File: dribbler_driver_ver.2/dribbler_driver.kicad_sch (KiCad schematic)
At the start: 93 parts, among them J1 SWD_Debug, J2 Conn_01x08, J3 Conn_01x02_MountingPin, J4 Conn_01x02_MountingPin, Q1 WSD4070DN, Q10 WSD4070DN, Q2 WSD4070DN, Q5 WSD4070DN, Q6 WSD4070DN, Q9 WSD4070DN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

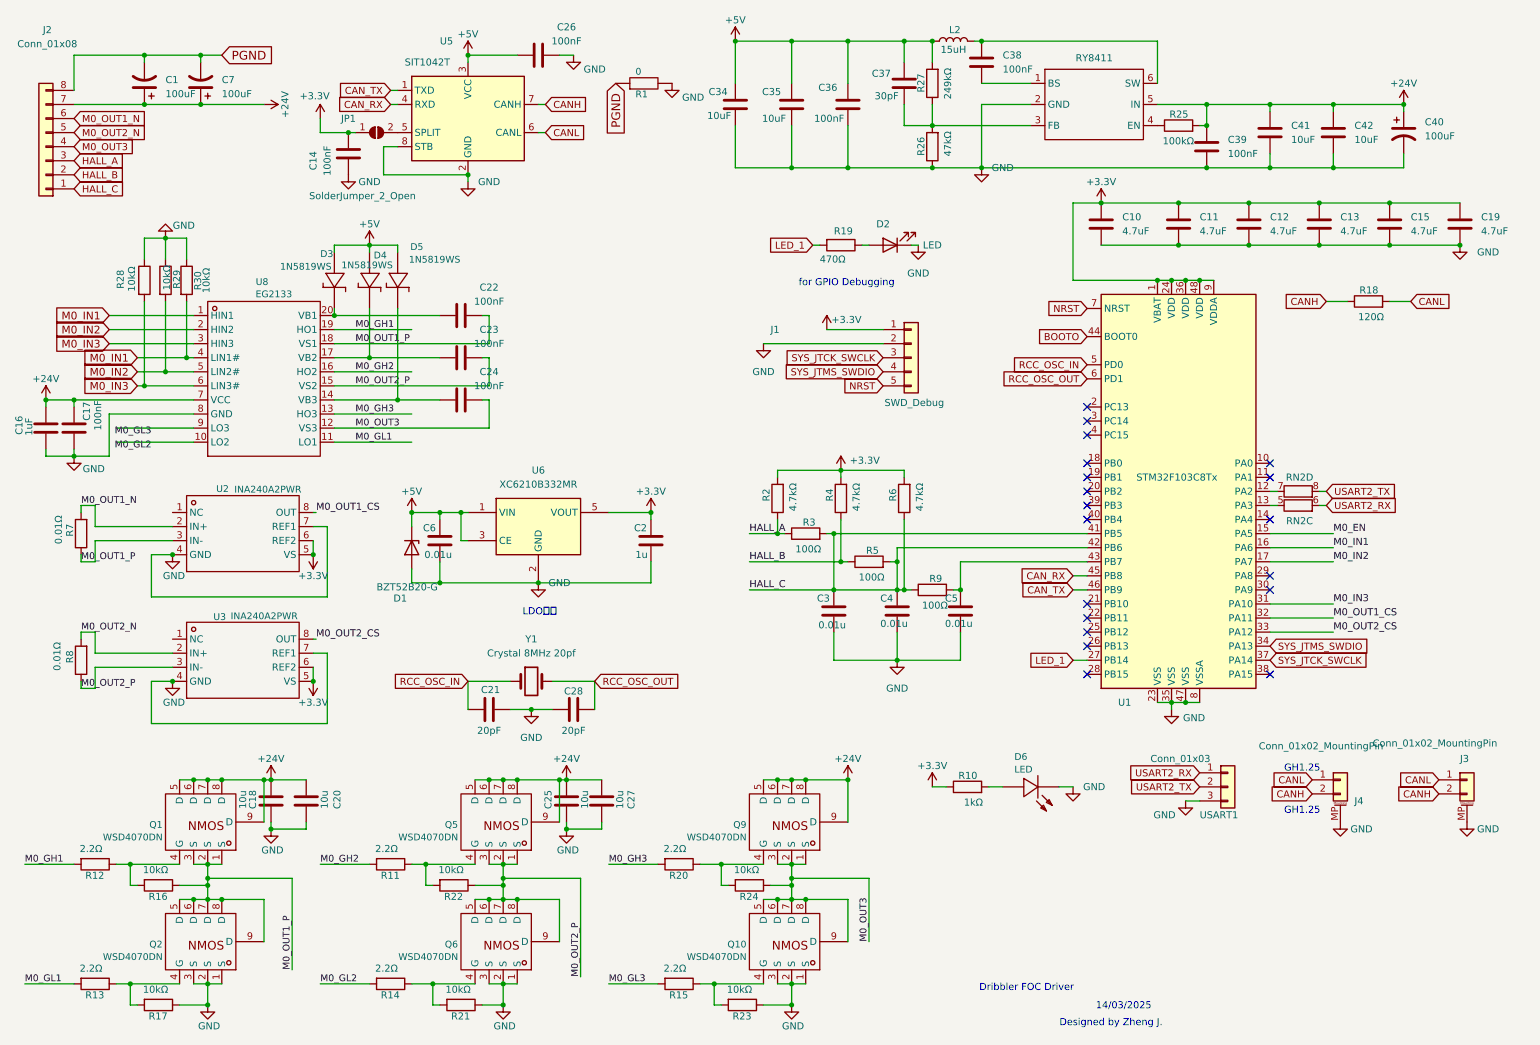
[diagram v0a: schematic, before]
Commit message: fixed stm32 peripherals
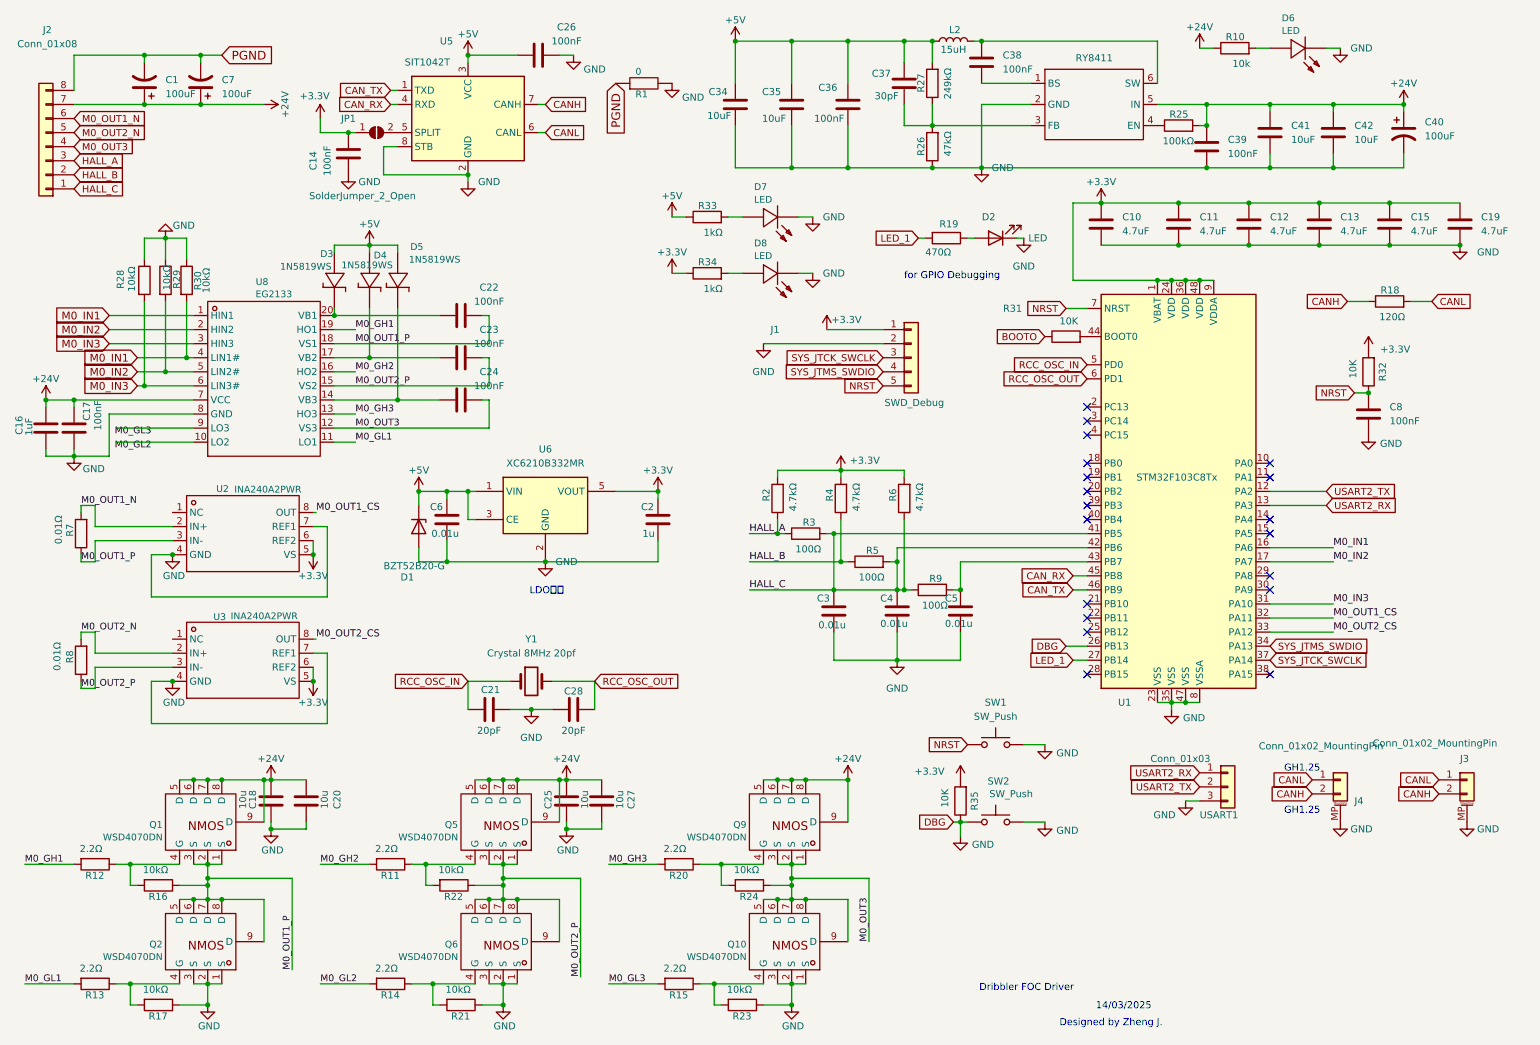
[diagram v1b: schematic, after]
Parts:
- removed RN2: R_Pack04_SIP_Split, R_array_4:0402*4_r, symbol Device:R_Pack04_SIP_Split
- added C8: 100nF, symbol Device:C
- added D7, D8: LED, LED_SMD:LED_0603_1608Metric_Pad1.05x0.95mm_HandSolder, symbol SCH_DengFO-easyedapro:17-21SUYC/TR8
- added R31, R32, R35: 10K, symbol Device:R
- added R33, R34: 1kΩ, Resistor_SMD:R_0603_1608Metric_Pad0.98x0.95mm_HandSolder, symbol Device:R
- added SW1, SW2: SW_Push, symbol Switch:SW_Push
- R10: value 1kΩ -> 10k
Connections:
- net +24V: now also R10.1
- net +3.3V: now also R32.2, R34.1, R35.2; no longer R10.1
- net +5V: now also R33.1
- net BOOTO: now also R31.1; no longer U1.44 (BOOT0)
- net GND: now also U1.26 (PB13), C8.2, D7.1 (-), D8.1 (-), R35.1, SW1.2, SW2.1, SW2.2
- net NRST: now also C8.1, R32.1, SW1.1
- net USART2_RX: now also U1.13 (PA3)
- net USART2_TX: now also U1.12 (PA2)
- net M0_EN: no longer names the net of U1.15 (PA5)
- new net: D8.2 (+), R34.2
- new net: D7.2 (+), R33.2
- new net: R31.2, U1.44 (BOOT0)
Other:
- moved on the sheet: C2, C6, D1, D2, D6, R10, R18, R19, U6
